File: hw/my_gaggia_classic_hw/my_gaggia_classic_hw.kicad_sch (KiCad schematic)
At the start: 19 parts, among them M1 Pump, Q1 NMOS, TN0702N3-G, SW1 Power switch, SW2 Coffee switch, U1 SSR G3NA, U2 SMT172, U3 2.2" color LCD

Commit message: add solid state relay for pump control
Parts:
- added Q2: NMOS, TN0702N3-G, symbol Simulation_SPICE:NMOS
- added U4: SSR D2410-10, symbol Relay_SolidState:S102S02
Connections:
- net +3.3V: now also SW2.2; no longer SW2.4
- net +5V: now also U4.3
- net 230V: now also U4.1; no longer SW2.2
- net COFFEE EXTRACT: now also SW2.1; no longer SW2.3
- net GND: now also Q2.3 (S)
- net at M1.1: now also U4.2; no longer SW2.1
- new net N PUMP ENABLE: Q2.2 (G)
- new net PUMP ENABLE: Q2.1 (D), U4.4
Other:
- moved on the sheet: Q1, SW2

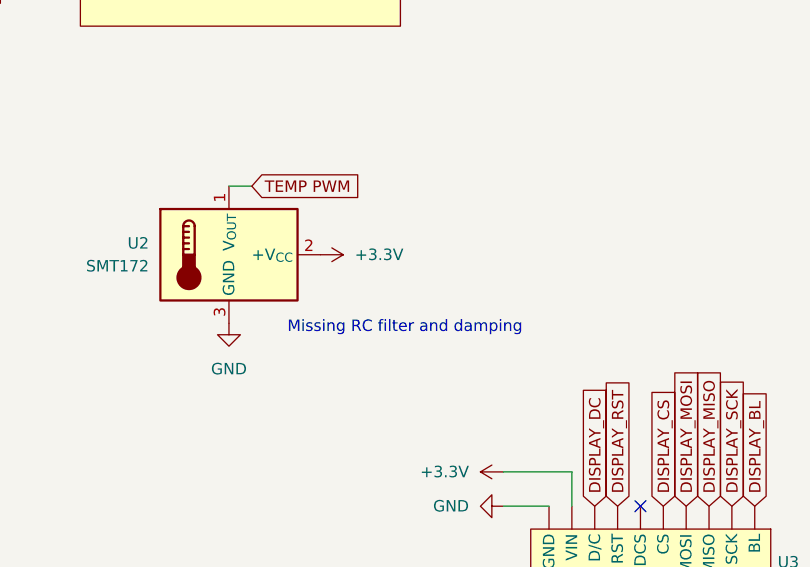
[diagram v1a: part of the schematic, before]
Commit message: add filter to temperature sensor
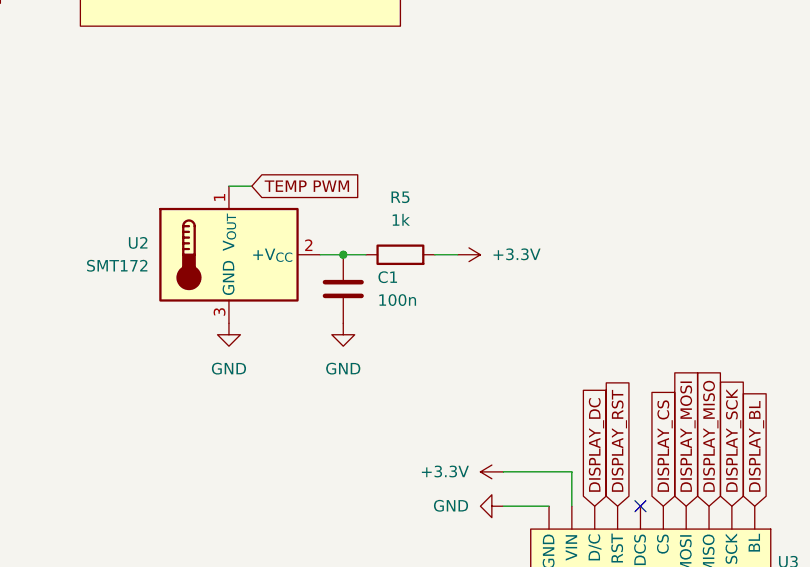
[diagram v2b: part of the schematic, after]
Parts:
- added C1: 100n, symbol Device:C
- added R5: 1k, symbol Device:R
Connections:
- net +3.3V: now also R5.2; no longer U2.2 (+V_{CC})
- net GND: now also C1.2
- new net: C1.1, R5.1, U2.2 (+V_{CC})
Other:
- note removed: "Missing RC filter and damping"
